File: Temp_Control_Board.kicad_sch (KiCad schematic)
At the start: 34 parts

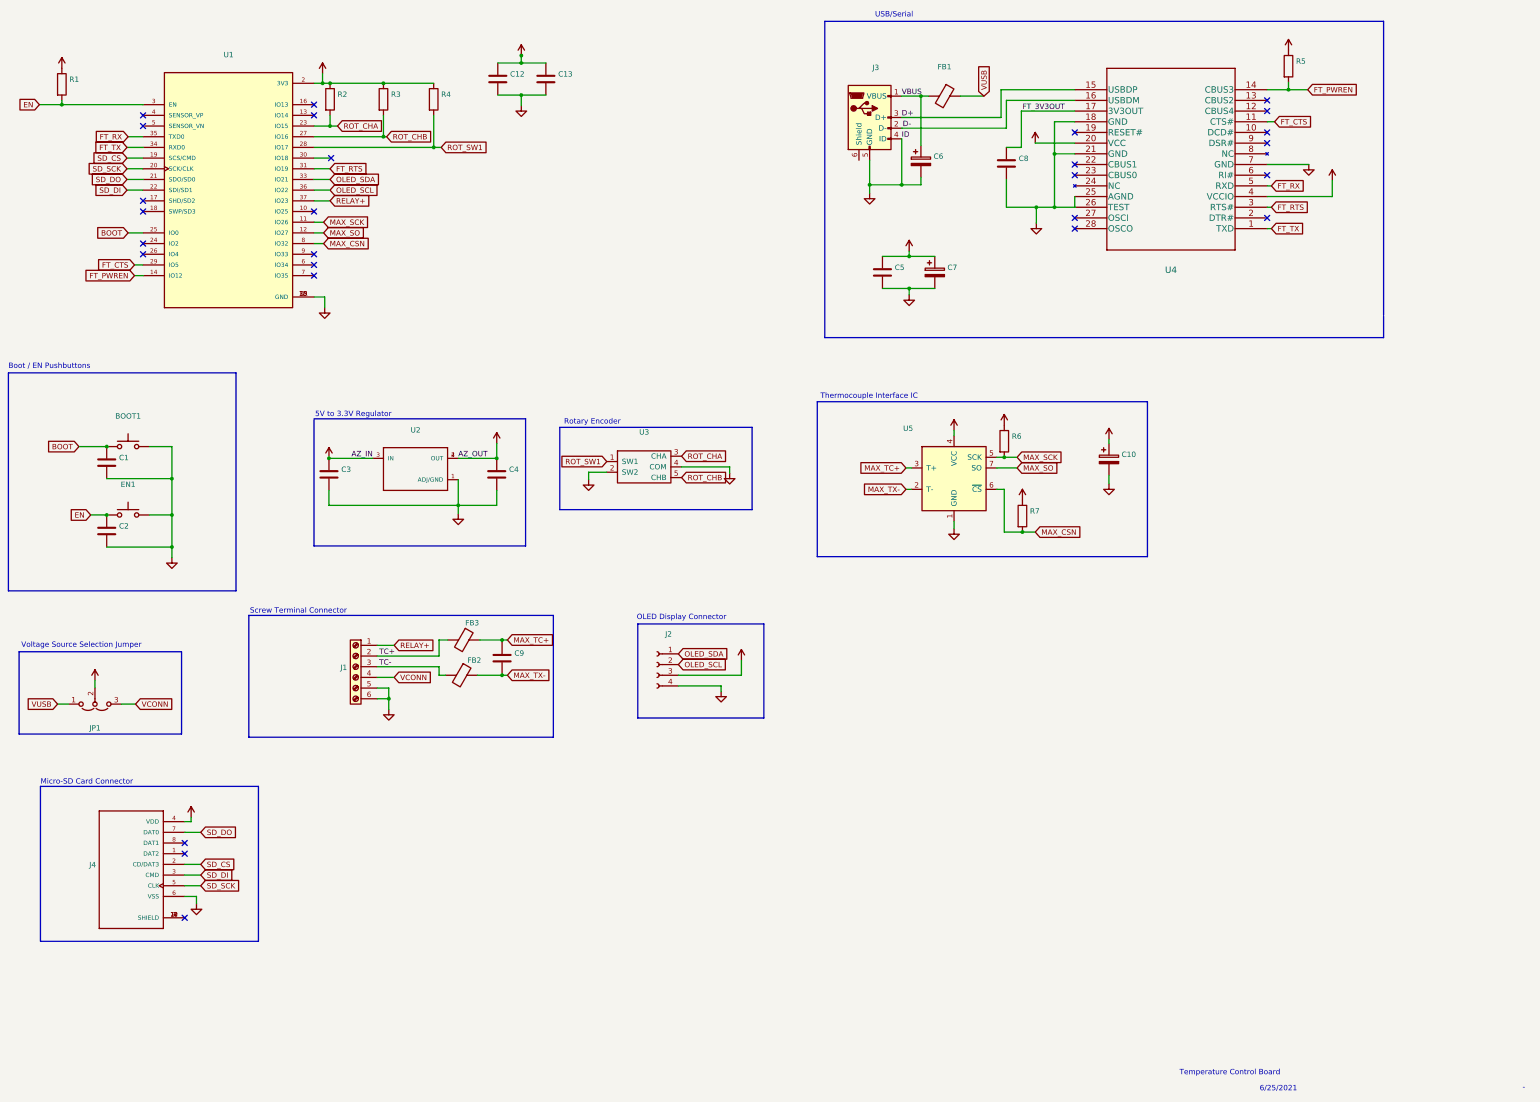
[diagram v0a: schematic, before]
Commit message: pcb/shc: Fixed tactile switch routing, tied USB shield to GND
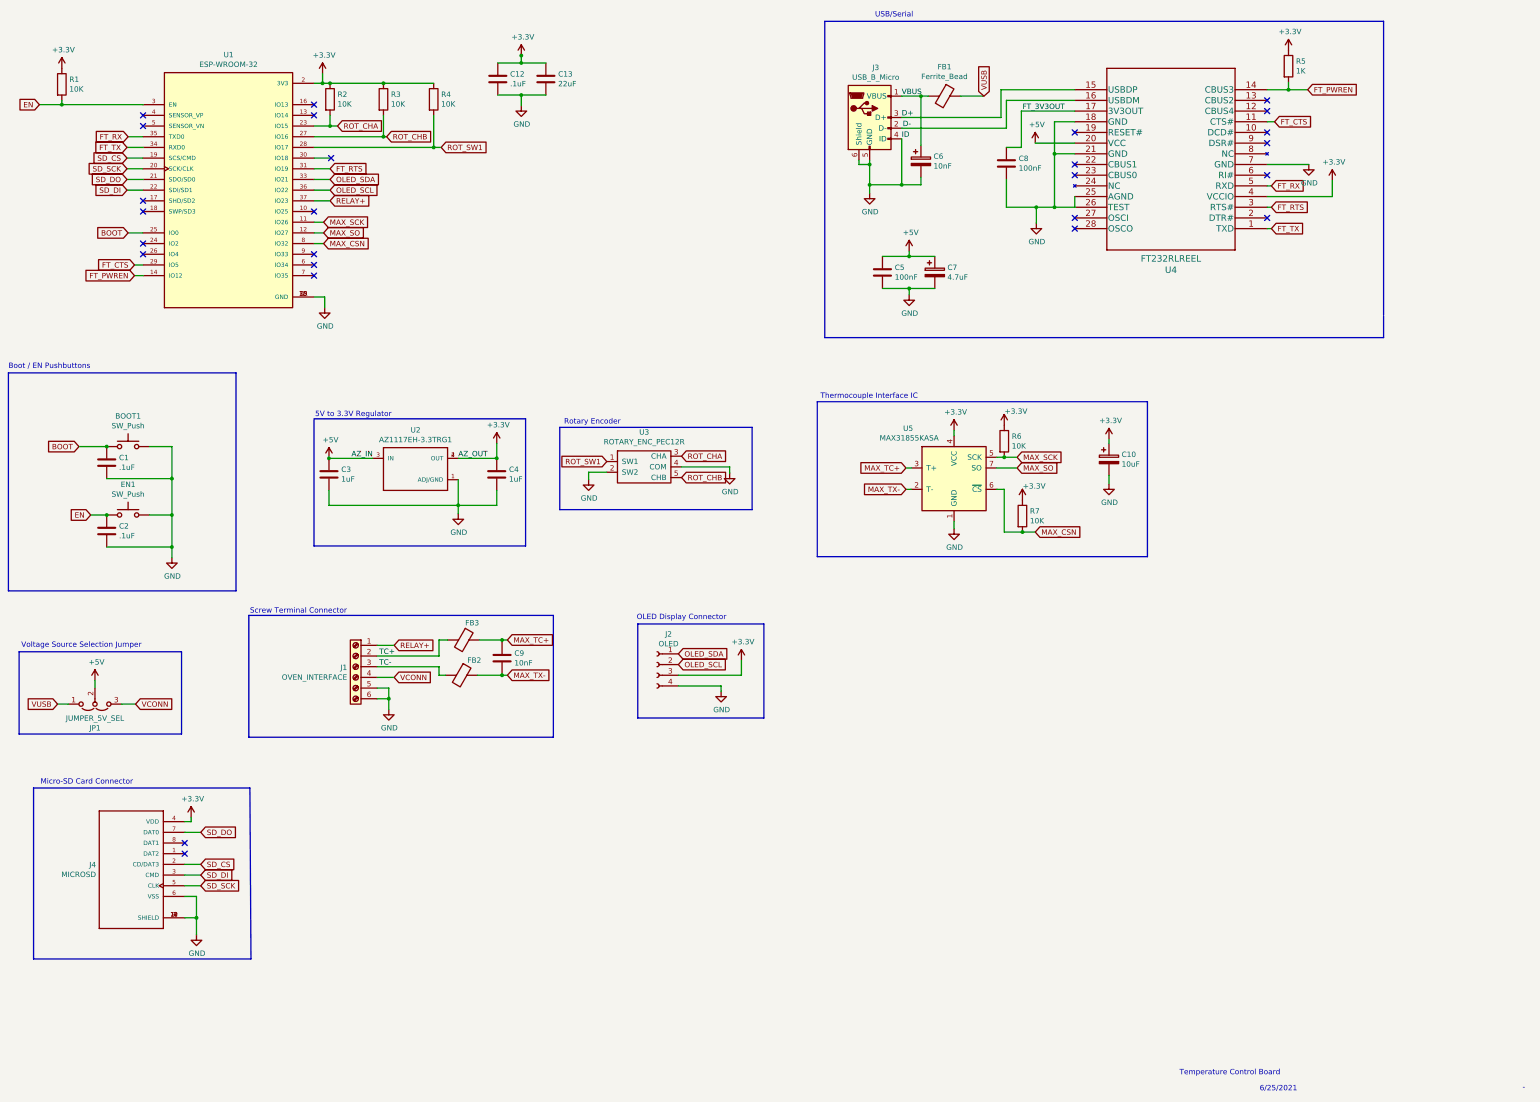
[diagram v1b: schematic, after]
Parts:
- BOOT1, EN1: value (none) -> SW_Push; footprint (none) -> tactile_switch:PTS645SK43SMTR92LF-CONNECTED
- C1, C12, C2: value (none) -> .1uF; footprint (none) -> Capacitor_SMD:C_0805_2012Metric_Pad1.15x1.40mm_HandSolder
- C10: value (none) -> 10uF; footprint (none) -> Capacitor_SMD:C_0805_2012Metric_Pad1.15x1.40mm_HandSolder
- C13: value (none) -> 22uF; footprint (none) -> Capacitor_SMD:C_0805_2012Metric_Pad1.15x1.40mm_HandSolder
- C3, C4: value (none) -> 1uF; footprint (none) -> Capacitor_SMD:C_0805_2012Metric_Pad1.15x1.40mm_HandSolder
- C5, C8: value (none) -> 100nF; footprint (none) -> Capacitor_SMD:C_0805_2012Metric_Pad1.15x1.40mm_HandSolder
- C6, C9: value (none) -> 10nF; footprint (none) -> Capacitor_SMD:C_0805_2012Metric_Pad1.15x1.40mm_HandSolder
- C7: value (none) -> 4.7uF; footprint (none) -> Capacitor_SMD:C_0805_2012Metric_Pad1.15x1.40mm_HandSolder
- FB1, FB2, FB3: value (none) -> Ferrite_Bead; footprint (none) -> Resistor_SMD:R_0805_2012Metric_Pad1.15x1.40mm_HandSolder
- J1: value (none) -> OVEN_INTERFACE; footprint (none) -> TerminalBlock:TerminalBlock_bornier-6_P5.08mm
- J2: value (none) -> OLED; footprint (none) -> Display:OLED_1MIL_HEADER_WHOLES
- J3: value (none) -> USB_B_Micro
- J4: value (none) -> MICROSD; footprint (none) -> microsd_connector:GCT_MEM2067-02-180-00-A_REVB
- JP1: value (none) -> JUMPER_5V_SEL; footprint (none) -> Jumper:SolderJumper-3_P1.3mm_Open_Pad1.0x1.5mm
- R1, R2, R3, R4, R6, R7: value (none) -> 10K; footprint (none) -> Resistor_SMD:R_0805_2012Metric_Pad1.15x1.40mm_HandSolder
- R5: value (none) -> 1K; footprint (none) -> Resistor_SMD:R_0805_2012Metric_Pad1.15x1.40mm_HandSolder
- U1: value (none) -> ESP-WROOM-32
- U2: value (none) -> AZ1117EH-3.3TRG1; footprint (none) -> 3V3_regulator:SOT230P700X180-4N
- U3: value (none) -> ROTARY_ENC_PEC12R; footprint (none) -> ROTARY_ENC_PEC12R:ROTARY_ENC_PEC12R
- U4: value (none) -> FT232RLREEL; footprint (none) -> ft232r:FT232RLREEL
- U5: value (none) -> MAX31855KASA; footprint (none) -> Package_SO:SOIC-8_3.9x4.9mm_P1.27mm
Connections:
- net GND: now also J3.6 (Shield), J4.10 (SHIELD), J4.11 (SHIELD), J4.12 (SHIELD), J4.9 (SHIELD)
- no-connect marks 27 -> 26

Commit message: Fixed BOOT / EN SWs ref designators
    - Fixes #4
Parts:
- J3: footprint (none) -> usb_connector:GCT_USB3076-XX-X_REVC
- SW1: renamed from BOOT1; value SW_Push -> BOOT
- SW2: renamed from EN1; value SW_Push -> EN
- U1: footprint (none) -> esp32:MODULE_ESP-WROOM-32
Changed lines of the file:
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@@
     (property "Reference" "U1" (id 0) (at 83.82 34.6202 0))
     (property "Value" "ESP-WROOM-32" (id 1) (at 83.82 36.9316 0))
-    (property "Footprint" "" (id 2) (at 83.82 66.802 0)
+    (property "Footprint" "esp32:MODULE_ESP-WROOM-32" (id 2) (at 83.82 66.802 0)
       (effects (font (size 1.27 1.27)) (justify left bottom) hide)
     )
@@
   (symbol (lib_id "Switch:SW_Push") (at 59.944 127.762 0) (unit 1)
     (in_bom yes) (on_board yes)
-    (property "Reference" "BOOT1" (id 0) (at 59.944 120.523 0))
-    (property "Value" "SW_Push" (id 1) (at 59.944 122.8344 0))
+    (property "Reference" "SW1" (id 0) (at 59.944 120.523 0))
+    (property "Value" "BOOT" (id 1) (at 59.944 122.8344 0))
     (property "Footprint" "tactile_switch:PTS645SK43SMTR92LF-CONNECTED" (id 2) (at 59.944 122.682 0)
       (effects (font (size 1.27 1.27)) hide)
@@
   (symbol (lib_id "Switch:SW_Push") (at 59.944 144.018 0) (unit 1)
     (in_bom yes) (on_board yes)
-    (property "Reference" "EN1" (id 0) (at 59.944 136.779 0))
-    (property "Value" "SW_Push" (id 1) (at 59.944 139.0904 0))
+    (property "Reference" "SW2" (id 0) (at 59.944 136.779 0))
+    (property "Value" "EN" (id 1) (at 59.944 139.0904 0))
     (property "Footprint" "tactile_switch:PTS645SK43SMTR92LF-CONNECTED" (id 2) (at 59.944 138.938 0)
       (effects (font (size 1.27 1.27)) hide)
@@
     (property "Reference" "J3" (id 0) (at 237.6678 37.6682 0))
     (property "Value" "USB_B_Micro" (id 1) (at 237.6678 39.9796 0))
-    (property "Footprint" "" (id 2) (at 240.03 50.8 0)
+    (property "Footprint" "usb_connector:GCT_USB3076-XX-X_REVC" (id 2) (at 240.03 50.8 0)
       (effects (font (size 1.27 1.27)) hide)
     )
@@
       (reference "#PWR0111") (unit 1) (value "GND") (footprint "")
     )
-    (path "/00000000-0000-0000-0000-0000607b30f3"
-      (reference "BOOT1") (unit 1) (value "SW_Push") (footprint "tactile_switch:PTS645SK43SMTR92LF-CONNECTED")
-    )
     (path "/00000000-0000-0000-0000-0000607d60a1"
       (reference "C1") (unit 1) (value ".1uF") (footprint "Capacitor_SMD:C_0805_2012Metric_Pad1.15x1.40mm_HandSolder")
@@
       (reference "C13") (unit 1) (value "22uF") (footprint "Capacitor_SMD:C_0805_2012Metric_Pad1.15x1.40mm_HandSolder")
     )
-    (path "/00000000-0000-0000-0000-0000607ca03c"
-      (reference "EN1") (unit 1) (value "SW_Push") (footprint "tactile_switch:PTS645SK43SMTR92LF-CONNECTED")
-    )
     (path "/00000000-0000-0000-0000-0000607f5acc"
       (reference "FB1") (unit 1) (value "Ferrite_Bead") (footprint "Resistor_SMD:R_0805_2012Metric_Pad1.15x1.40mm_HandSolder")
@@
       (reference "R7") (unit 1) (value "10K") (footprint "Resistor_SMD:R_0805_2012Metric_Pad1.15x1.40mm_HandSolder")
     )
+    (path "/00000000-0000-0000-0000-0000607b30f3"
+      (reference "SW1") (unit 1) (value "BOOT") (footprint "tactile_switch:PTS645SK43SMTR92LF-CONNECTED")
+    )
+    (path "/00000000-0000-0000-0000-0000607ca03c"
+      (reference "SW2") (unit 1) (value "EN") (footprint "tactile_switch:PTS645SK43SMTR92LF-CONNECTED")
+    )
     (path "/00000000-0000-0000-0000-0000607af546"

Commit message: Changed all .1uF cap values to 100nF for consistency
    - Fixes #5
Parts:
- C1, C12, C2: value .1uF -> 100nF
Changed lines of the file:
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@@
       (effects (font (size 1.27 1.27)) (justify left))
     )
-    (property "Value" ".1uF" (id 1) (at 57.785 132.715 0)
+    (property "Value" "100nF" (id 1) (at 57.785 132.715 0)
       (effects (font (size 1.27 1.27)) (justify left))
     )
@@
       (effects (font (size 1.27 1.27)) (justify left))
     )
-    (property "Value" ".1uF" (id 1) (at 57.785 148.971 0)
+    (property "Value" "100nF" (id 1) (at 57.785 148.971 0)
       (effects (font (size 1.27 1.27)) (justify left))
     )
@@
       (effects (font (size 1.27 1.27)) (justify left))
     )
-    (property "Value" ".1uF" (id 1) (at 150.749 41.529 0)
+    (property "Value" "100nF" (id 1) (at 150.749 41.529 0)
       (effects (font (size 1.27 1.27)) (justify left))
     )
@@
     )
     (path "/00000000-0000-0000-0000-0000607d60a1"
-      (reference "C1") (unit 1) (value ".1uF") (footprint "Capacitor_SMD:C_0805_2012Metric_Pad1.15x1.40mm_HandSolder")
+      (reference "C1") (unit 1) (value "100nF") (footprint "Capacitor_SMD:C_0805_2012Metric_Pad1.15x1.40mm_HandSolder")
     )
     (path "/00000000-0000-0000-0000-0000607d89f7"
-      (reference "C2") (unit 1) (value ".1uF") (footprint "Capacitor_SMD:C_0805_2012Metric_Pad1.15x1.40mm_HandSolder")
+      (reference "C2") (unit 1) (value "100nF") (footprint "Capacitor_SMD:C_0805_2012Metric_Pad1.15x1.40mm_HandSolder")
     )
     (path "/00000000-0000-0000-0000-0000607cc4d0"
@@
     )
     (path "/00000000-0000-0000-0000-000060dec276"
-      (reference "C12") (unit 1) (value ".1uF") (footprint "Capacitor_SMD:C_0805_2012Metric_Pad1.15x1.40mm_HandSolder")
+      (reference "C12") (unit 1) (value "100nF") (footprint "Capacitor_SMD:C_0805_2012Metric_Pad1.15x1.40mm_HandSolder")
     )
     (path "/00000000-0000-0000-0000-000060df3b37"
